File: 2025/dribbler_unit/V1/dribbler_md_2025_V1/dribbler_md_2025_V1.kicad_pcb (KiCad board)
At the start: 2 copper layers, 78 parts, among them J2 Conn_01x07_Pin, J4 Conn_01x02_Pin, J5 Conn_01x02_Pin, J6 Conn_01x04_Pin, U1 MAX3051, U2 DRV8701, U3 STM32F446RETx

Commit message: 回路図完了
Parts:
- added J1: Conn_01x02_Pin, dribbler_md:XT30, F.Cu at (138.5, 53.3)
- added J3: Conn_01x02_Pin, dribbler_md:XT30, F.Cu at (145.2, 53.3)
- added R34: 10k, Resistor_SMD:R_0603_1608Metric_Pad0.98x0.95mm_HandSolder, F.Cu at (128.2, 62.1)
- added SW1: SW_Wuerth_450301014042, dribbler_md:IS-1235-G, F.Cu at (109.9, 108.2)
- added SW2: SW_Wuerth_450301014042, dribbler_md:IS-1235-G, F.Cu at (123.2, 108.2)
- added SW3: SW_MEC_5E, dribbler_md:TS-06104, F.Cu at (146.1, 62.5)
- added SW4: SW_Wuerth_450301014042, dribbler_md:IS-1235-G, F.Cu at (135.4, 72.0)
- added SW5: SW_MEC_5E, dribbler_md:TS-06104, F.Cu at (146.1, 69.9)
- added Y1: Crystal_GND2, dribbler_md:CSTNE16M0V530000R0, F.Cu at (124.9, 90.7)
- moved R14 53.2 mm to (176.0, 78.5)
- moved REG1 48.9 mm to (165.1, 95.2)
- moved U2 47.5 mm to (171.6, 70.6)
- moved C3 43.7 mm to (182.5, 86.5)
- moved C2 42.3 mm to (182.5, 58.5)
- moved FET4 40.9 mm to (184.0, 77.7)
- moved FET1 40.6 mm to (183.6, 67.3)
- moved FET2 40.3 mm to (183.4, 71.0)
- moved J2 40.0 mm to (138.1, 43.5)
- moved FET3 39.8 mm to (183.0, 74.7)
- moved J6 29.7 mm to (143.4, 90.8)
- moved J4 28.4 mm to (154.6, 61.6)
- moved J5 28.4 mm to (154.6, 68.1)
- moved C13 26.7 mm to (132.8, 54.3)
- moved C4 26.7 mm to (132.8, 42.3)
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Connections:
- net SN renamed GND_main
- C1 pad 2: MD_SO -> GND_log
- C10 pad 1: MD_SO -> GND_log
- C15 pad 2: MD_SO -> GND_log
- C16 pad 2: MD_SO -> GND_log
- C17 pad 2: MD_SO -> GND_log
- C18 pad 2: MD_SO -> GND_log
- C19 pad 2: MD_SO -> GND_log
- C20 pad 2: MD_SO -> GND_log
- C21 pad 2: MD_SO -> GND_log
- C22 pad 1: MD_SO -> GND_log
- C23 pad 2: MD_SO -> GND_log
- C24 pad 2: MD_SO -> GND_log
- C6 pad 2: MD_SO -> GND_log
- C7 pad 2: MD_SO -> GND_log
- C8 pad 2: MD_SO -> GND_log
- C9 pad 2: MD_SO -> GND_log
- D4 pad 1: MD_SO -> GND_log
- D5 pad 1: MD_SO -> GND_log
- D6 pad 1: MD_SO -> GND_log
- D7 pad 1: MD_SO -> GND_log
- J2 pad 7: MD_SO -> GND_log
- R1 pad 1: MD_SO -> GND_log
- R18 pad 2: MD_SO -> GND_log
- R19 pad 2: MD_SO -> GND_log
- R2 pad 1: MD_SO -> GND_log
- R32 pad 2: MD_SO -> GND_log
- U1 pad 2: MD_SO -> GND_log
- U1 pad 5: MD_SO -> GND_log
- U1 pad 8: MD_SO -> GND_log
- U2 pad 16: MD_SO -> GND_log
- U2 pad 25: MD_SO -> GND_log
- U2 pad 5: MD_SO -> GND_log
- U3 pad 12: MD_SO -> GND_log
- U3 pad 18: MD_SO -> GND_log
- U3 pad 31: MD_SO -> GND_log
- U3 pad 47: MD_SO -> GND_log
- U3 pad 63: MD_SO -> GND_log

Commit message: FET再選定
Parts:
- removed FET1, FET2, FET3, FET4: MCMN2012A-TP, dribbler_md:MCMN2012A
- added C25: 10u, Capacitor_SMD:C_0805_2012Metric_Pad1.18x1.45mm_HandSolder, F.Cu at (197.1, 94.4)
- added C26: 10u, Capacitor_SMD:C_0805_2012Metric_Pad1.18x1.45mm_HandSolder, F.Cu at (197.1, 97.4)
- added C27: 4.7u, Capacitor_SMD:C_0603_1608Metric_Pad1.08x0.95mm_HandSolder, F.Cu at (186.2, 79.7)
- added C28: 0.1u, Capacitor_SMD:C_0603_1608Metric_Pad1.08x0.95mm_HandSolder, F.Cu at (186.2, 82.2)
- added C29: 0.1u, Capacitor_SMD:C_0603_1608Metric_Pad1.08x0.95mm_HandSolder, F.Cu at (186.2, 84.7)
- added C30: 0.1u, Capacitor_SMD:C_0603_1608Metric_Pad1.08x0.95mm_HandSolder, F.Cu at (186.2, 87.2)
- added C31: 0.1u, Capacitor_SMD:C_0603_1608Metric_Pad1.08x0.95mm_HandSolder, F.Cu at (186.2, 89.7)
- added C32: 0.1u, Capacitor_SMD:C_0603_1608Metric_Pad1.08x0.95mm_HandSolder, F.Cu at (186.2, 92.2)
- added C33: 0.1u, Capacitor_SMD:C_0603_1608Metric_Pad1.08x0.95mm_HandSolder, F.Cu at (186.2, 94.8)
- added C34: 4.7u, Capacitor_SMD:C_0603_1608Metric_Pad1.08x0.95mm_HandSolder, F.Cu at (186.2, 97.3)
- added C35: 0.1u, Capacitor_SMD:C_0603_1608Metric_Pad1.08x0.95mm_HandSolder, F.Cu at (186.2, 99.8)
- added C36: 0.1u, Capacitor_SMD:C_0603_1608Metric_Pad1.08x0.95mm_HandSolder, F.Cu at (186.2, 102.3)
- added U4: DRV8701, Package_DFN_QFN:VQFN-24-1EP_4x4mm_P0.5mm_EP2.5x2.5mm, F.Cu at (220.2, 118.8)
- added U5: STM32F446RETx, Package_QFP:LQFP-64_10x10mm_P0.5mm, F.Cu at (195.6, 85.7)
- C10: value 1u -> 10u; footprint Capacitor_SMD:C_0603_1608Metric_Pad1.08x0.95mm_HandSolder -> Capacitor_SMD:C_0805_2012Metric_Pad1.18x1.45mm_HandSolder
- C11, C16, C18, C19, C20, C6, C7: value 0.1u -> 10u; footprint Capacitor_SMD:C_0603_1608Metric_Pad1.08x0.95mm_HandSolder -> Capacitor_SMD:C_0805_2012Metric_Pad1.18x1.45mm_HandSolder
- C12: value 1000pf -> 10u; footprint Capacitor_SMD:C_0603_1608Metric_Pad1.08x0.95mm_HandSolder -> Capacitor_SMD:C_0805_2012Metric_Pad1.18x1.45mm_HandSolder
- C14: value 10u -> 0.1u; footprint Capacitor_SMD:C_0805_2012Metric_Pad1.18x1.45mm_HandSolder -> Capacitor_SMD:C_0603_1608Metric_Pad1.08x0.95mm_HandSolder
- C15: value 4.7u -> 10u; footprint Capacitor_SMD:C_0603_1608Metric_Pad1.08x0.95mm_HandSolder -> Capacitor_SMD:C_0805_2012Metric_Pad1.18x1.45mm_HandSolder
- C2, C3: value 470u -> 10u; footprint Capacitor_SMD:CP_Elec_10x10 -> Capacitor_SMD:C_0805_2012Metric_Pad1.18x1.45mm_HandSolder
- C21: footprint Capacitor_SMD:C_0603_1608Metric_Pad1.08x0.95mm_HandSolder -> Capacitor_SMD:C_0805_2012Metric_Pad1.18x1.45mm_HandSolder
- C22: value 4.7u -> 1u
- C24: value 0.1u -> 1000pf
- C4, C5: value 1u -> 10u
- C9: value 0.1u -> 10u
- F1, F2, REG1: moved to B.Cu
- R1, R10, R13, R15, R2, R3, R4, R5, R6, R7, R8: footprint Resistor_SMD:R_0603_1608Metric_Pad0.98x0.95mm_HandSolder -> Resistor_SMD:R_0402_1005Metric_Pad0.72x0.64mm_HandSolder
- R11, R9: value 10k -> 200; footprint Resistor_SMD:R_0603_1608Metric_Pad0.98x0.95mm_HandSolder -> Resistor_SMD:R_0402_1005Metric_Pad0.72x0.64mm_HandSolder
- R12: value 200 -> 10k; footprint Resistor_SMD:R_0603_1608Metric_Pad0.98x0.95mm_HandSolder -> Resistor_SMD:R_0402_1005Metric_Pad0.72x0.64mm_HandSolder
- R14: value 0.04 -> 10k; footprint Resistor_SMD:R_2512_6332Metric_Pad1.40x3.35mm_HandSolder -> Resistor_SMD:R_0402_1005Metric_Pad0.72x0.64mm_HandSolder; moved to B.Cu
- R16: value 200 -> 0.04; footprint Resistor_SMD:R_0603_1608Metric_Pad0.98x0.95mm_HandSolder -> Resistor_SMD:R_2512_6332Metric_Pad1.40x3.35mm_HandSolder
- R18: value 0 -> 10k
- R22: value 10k -> 0
- R25: value 1k -> 10k; footprint Resistor_SMD:R_0603_1608Metric_Pad0.98x0.95mm_HandSolder -> Resistor_SMD:R_0402_1005Metric_Pad0.72x0.64mm_HandSolder
- R26: value 2k -> 1k
- R27: value 10k -> 2k
- R28: value 1k -> 10k
- R32: value 10k -> 1k
- U2: value DRV8701 -> STS8DN3LLH5; footprint Package_DFN_QFN:VQFN-24-1EP_4x4mm_P0.5mm_EP2.5x2.5mm -> Package_SO:SO-8_3.9x4.9mm_P1.27mm
- U3: value STM32F446RETx -> STS8DN3LLH5; footprint Package_QFP:LQFP-64_10x10mm_P0.5mm -> Package_SO:SO-8_3.9x4.9mm_P1.27mm
- moved R11 129.9 mm to (216.0, 144.1), turned to 90 degrees
- moved R16 128.2 mm to (204.3, 141.8)
- moved R10 127.1 mm to (212.6, 141.1), turned to -90 degrees
- moved R8 126.4 mm to (216.0, 131.2), turned to 90 degrees
- moved R9 125.9 mm to (212.6, 136.9), turned to -90 degrees
- moved C1 121.7 mm to (165.4, 150.8), turned to -90 degrees
- moved R15 121.0 mm to (212.0, 142.7), turned to 180 degrees
- moved R13 119.9 mm to (212.0, 138.5), turned to 180 degrees
- moved R12 119.7 mm to (216.6, 129.7)
- moved R5 114.7 mm to (156.4, 150.6), turned to 90 degrees
- moved R28 114.2 mm to (162.5, 155.9), turned to 180 degrees
- moved R29 113.3 mm to (162.5, 157.6), turned to 180 degrees
- moved R30 101.6 mm to (177.7, 140.8)
- moved R31 101.6 mm to (177.7, 143.3)
- moved J2 101.5 mm to (152.5, 144.0), turned to 90 degrees
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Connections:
- C10 pad 1: GND_log -> 18V_main
- C10 pad 2: Net-(U2-VCP) -> GND_main
- C11 pad 1: Net-(U2-CPH) -> 18V_main
- C11 pad 2: Net-(U2-CPL) -> GND_main
- C12 pad 1: SP -> 18V_main
- C13 pad 1: Net-(REG1-VIN) -> 18V_main
- C13 pad 2: GND_REG -> GND_main
- C14 pad 1: 3.3V_sub -> Net-(U4-AVDD)
- C14 pad 2: GND_REG -> GND_log
- C15 pad 1: Net-(U3-VCAP_1) -> 18V_main
- C15 pad 2: GND_log -> GND_main
- C16 pad 1: 3.3V_sub -> 18V_main
- C16 pad 2: GND_log -> GND_main
- C17 pad 1: 3.3V_sub -> Net-(U4-DVDD)
- C18 pad 1: 3.3V_sub -> 18V_main
- C18 pad 2: GND_log -> GND_main
- C19 pad 1: 3.3V_sub -> 18V_main
- C19 pad 2: GND_log -> GND_main
- C20 pad 1: 3.3V_sub -> 18V_main
- C21 pad 1: 3.3V_sub -> 18V_main
- C22 pad 2: 3.3V_sub -> Net-(U4-VCP)
- C23 pad 1: NRST -> Net-(U4-CPH)
- C23 pad 2: GND_log -> Net-(U4-CPL)
- C24 pad 1: USER_SW -> SP
- C24 pad 2: GND_log -> GND_main
- C6 pad 1: Net-(U2-AVDD) -> 18V_main
- C6 pad 2: GND_log -> GND_main
- C7 pad 1: Net-(U2-DVDD) -> 18V_main
- C7 pad 2: GND_log -> GND_main
- C8 pad 2: GND_log -> GND_main
- C9 pad 2: GND_log -> GND_main
- R10 pad 1: SP -> Net-(U2-G2)
- R10 pad 2: Net-(FET3-gate) -> SP
- R11 pad 1: SH1 -> Net-(U2-G2)
- R11 pad 2: Net-(FET4-gate) -> GL2
- R12 pad 1: Net-(FET1-gate) -> Net-(U3-G1)
- R12 pad 2: GH2 -> SP
- R13 pad 1: Net-(FET2-gate) -> Net-(U3-G1)
- R13 pad 2: GL2 -> GL1
- R14 pad 1: SP -> Net-(U3-G2)
- R14 pad 2: GND_main -> SH1
- R15 pad 1: Net-(FET3-gate) -> Net-(U3-G2)
- R15 pad 2: GL1 -> GH1
- R16 pad 1: Net-(FET4-gate) -> SP
- R16 pad 2: GH1 -> GND_main
- R17 pad 1: Net-(U2-SO) -> Net-(U4-SO)
- R18 pad 1: GND_main -> MD_SO
- R20 pad 2: GND_REG -> GND_log
- R22 pad 2: ENC_1 -> GND_REG
- R23 pad 1: ENC_2 -> GND_main
- R23 pad 2: GND_main -> ENC_1
- R24 pad 1: 3.3V_sub -> ENC_2
- R24 pad 2: NRST -> GND_main
- R25 pad 2: Net-(D1-A) -> NRST
- R26 pad 1: 6.5V_main -> 3.3V_sub
- R26 pad 2: Net-(D2-A) -> Net-(D1-A)
- R27 pad 1: 18V_main -> 6.5V_main
- R27 pad 2: Net-(D3-A) -> Net-(D2-A)
- R28 pad 1: USER_LED_1 -> 18V_main
- R28 pad 2: Net-(D4-A) -> Net-(D3-A)
- R29 pad 1: USER_LED_2 -> USER_LED_1
- R29 pad 2: Net-(D5-A) -> Net-(D4-A)
- R3 pad 2: Net-(U2-AVDD) -> Net-(U4-AVDD)
- R30 pad 1: GL2 -> USER_LED_2
- R30 pad 2: Net-(D6-A) -> Net-(D5-A)
- R31 pad 1: GL1 -> GL2
- R31 pad 2: Net-(D7-A) -> Net-(D6-A)
- R32 pad 1: BOOT -> GL1
- R32 pad 2: GND_log -> Net-(D7-A)
- R33 pad 1: 3.3V_sub -> BOOT
- R33 pad 2: USER_SW -> GND_log
- R34 pad 1: MD_SO -> 3.3V_sub
- R34 pad 2: GND_log -> USER_SW
- R4 pad 2: Net-(U2-AVDD) -> Net-(U4-AVDD)
- R6 pad 1: Net-(U2-nFAULT) -> Net-(U4-nFAULT)
- R7 pad 2: Net-(U2-SNSOUT) -> Net-(U4-SNSOUT)
- R8 pad 1: SH2 -> Net-(U2-G1)
- R8 pad 2: Net-(FET1-gate) -> SH2
- R9 pad 1: SP -> Net-(U2-G1)
- R9 pad 2: Net-(FET2-gate) -> GH2
- U2 pad 1: 18V_main -> SH2
- U2 pad 2: Net-(U2-VCP) -> Net-(U2-G1)
- U2 pad 3: Net-(U2-CPH) -> SP
- U2 pad 4: Net-(U2-CPL) -> Net-(U2-G2)
- U2 pad 5: GND_log -> SH2
- U2 pad 6: MD_VREF -> SH2
- U2 pad 7: Net-(U2-AVDD) -> 18V_main
- U2 pad 8: Net-(U2-DVDD) -> 18V_main
- U3 pad 1: 3.3V_sub -> SP
- U3 pad 2: unconnected-(U3-PC13-Pad2) -> Net-(U3-G1)
- U3 pad 3: unconnected-(U3-PC14-Pad3) -> SH1
- U3 pad 4: unconnected-(U3-PC15-Pad4) -> Net-(U3-G2)
- U3 pad 5: Net-(U3-PH0) -> 18V_main
- U3 pad 6: Net-(U3-PH1) -> 18V_main
- U3 pad 7: NRST -> SH1
- U3 pad 8: unconnected-(U3-PC0-Pad8) -> SH1
- Y1 pad 1: Net-(U3-PH0) -> Net-(U5-PH0)
- Y1 pad 3: Net-(U3-PH1) -> Net-(U5-PH1)
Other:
- board outline added: 50 x 50 mm

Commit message: FET周りを配線
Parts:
- added REF**: m2 hole, dribbler_md:m2 hole, F.Cu at (187.0, 103.0)
- added REF**: m2 hole, dribbler_md:m2 hole, F.Cu at (143.0, 147.0)
- added REF**: m2 hole, dribbler_md:m2 hole, F.Cu at (187.0, 147.0)
- added REF**: m2 hole, dribbler_md:m2 hole, F.Cu at (143.0, 103.0)
- F1, F2, R14, REG1: moved to F.Cu
- moved C1 121.4 mm to (88.6, 56.8), turned to 0 degrees
- moved R29 117.7 mm to (101.7, 56.8), turned to 0 degrees
- moved R31 111.5 mm to (101.7, 61.8)
- moved R30 111.5 mm to (101.7, 59.3)
- moved R28 102.5 mm to (97.3, 76.9), turned to 0 degrees
- moved C30 98.0 mm to (93.0, 56.8)
- moved C31 98.0 mm to (93.0, 59.3)
- moved C32 98.0 mm to (93.0, 61.8)
- moved C33 98.0 mm to (93.0, 64.3)
- moved C34 98.0 mm to (93.0, 66.8)
- moved C35 98.0 mm to (93.0, 69.3)
- moved C36 98.0 mm to (93.0, 71.8)
- moved C27 97.9 mm to (88.6, 71.8)
- moved C28 97.9 mm to (88.6, 74.3)
- moved C29 97.9 mm to (88.6, 76.9)
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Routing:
- net Net-(U2-G2): track 0.00 -> 4.11 mm
- net Net-(U3-G1): track 0.00 -> 4.11 mm
- net Net-(U3-G2): track 0.00 -> 4.11 mm
- net Net-(U2-G1): track 0.00 -> 4.11 mm
- added copper zone on F.Cu, net 18V_main
- added copper zone on F.Cu, net SH1
- added copper zone on F.Cu, net SH2
- added copper zone on F.Cu, net SP

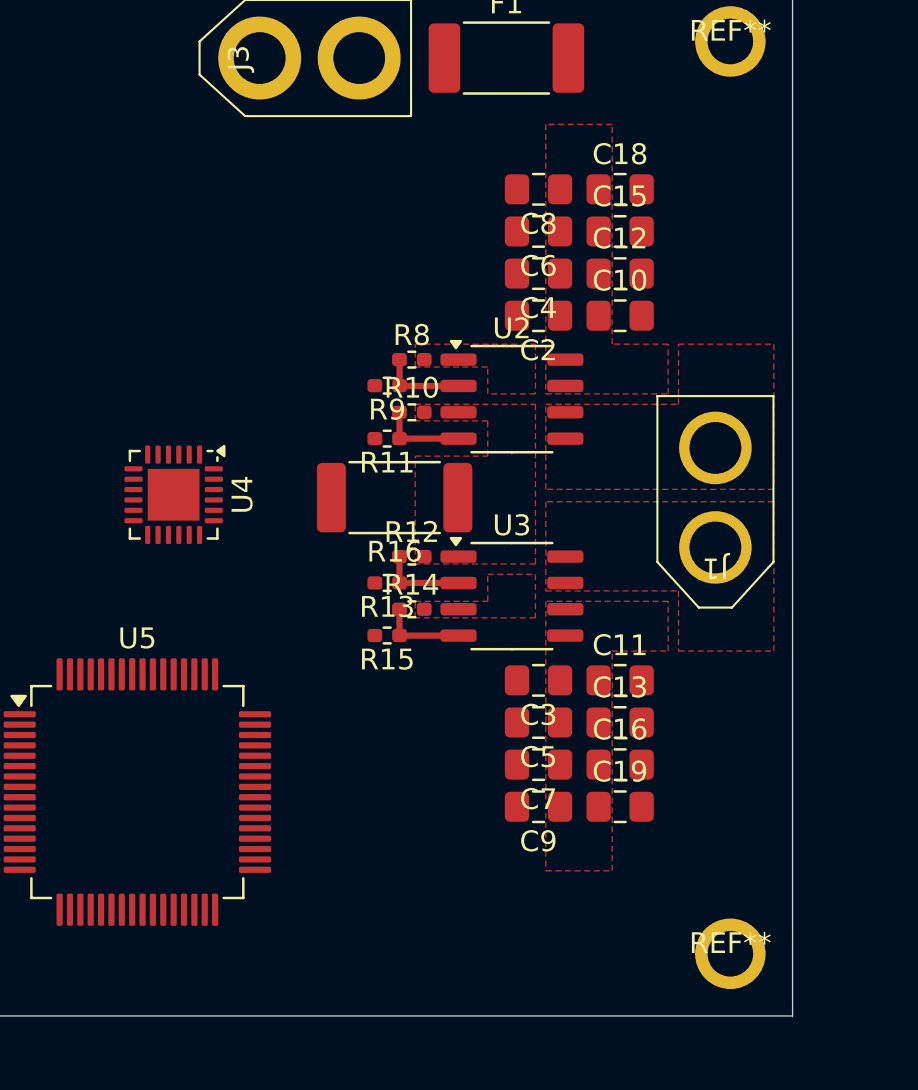
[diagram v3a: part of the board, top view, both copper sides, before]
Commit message: FET周りを配線-2
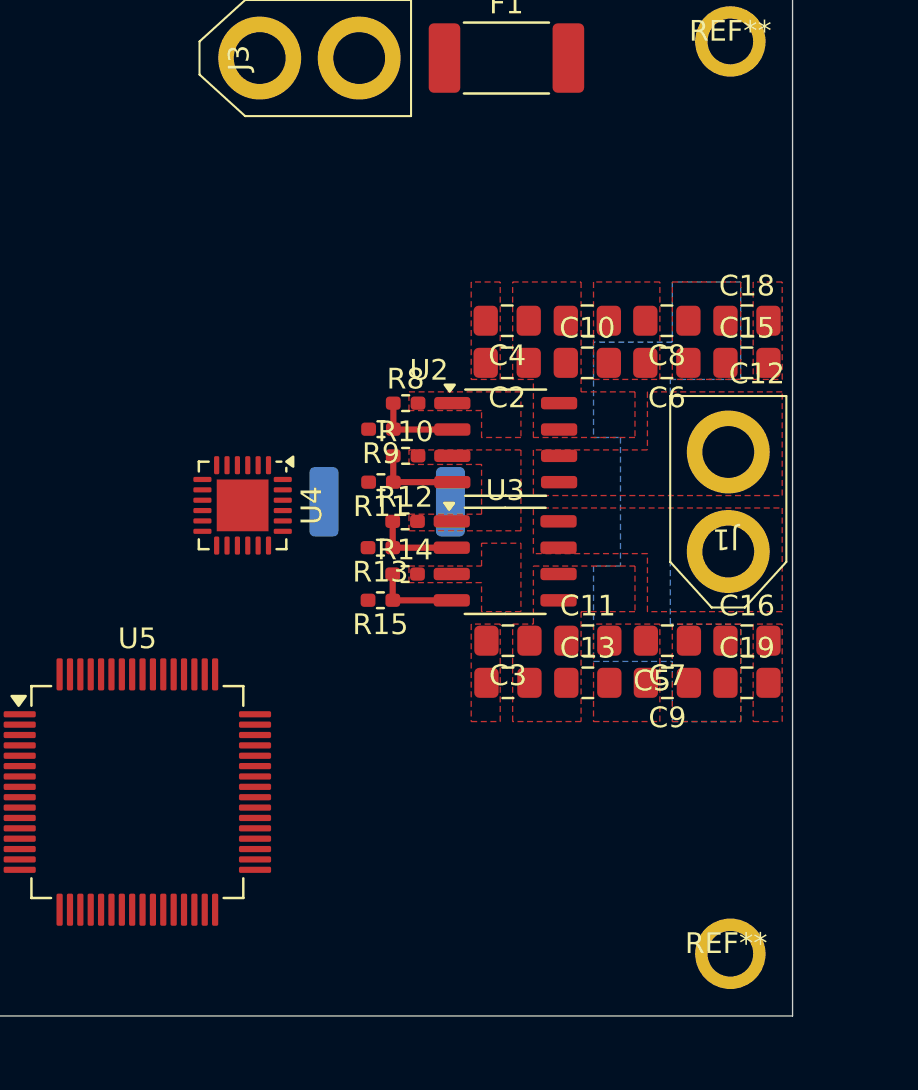
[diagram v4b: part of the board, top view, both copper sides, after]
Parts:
- R16: moved to B.Cu
- moved C6 8.86 mm to (183.9, 118.5)
- moved C8 8.86 mm to (183.9, 116.5)
- moved C15 8.81 mm to (187.8, 118.5)
- moved C18 8.81 mm to (187.8, 116.5)
- moved C7 8.62 mm to (184.0, 131.9)
- moved C9 8.62 mm to (184.0, 133.9)
- moved C16 8.55 mm to (187.8, 131.9)
- moved C19 8.55 mm to (187.8, 133.9)
- moved U4 3.36 mm to (163.5, 125.4)
- moved C10 2.77 mm to (180.1, 118.5)
- moved C12 2.77 mm to (180.1, 116.5)
- moved C2 2.73 mm to (176.2, 118.5)
- moved C4 2.73 mm to (176.2, 116.5)
- moved C13 2.47 mm to (180.1, 133.9)
- moved C11 2.47 mm to (180.1, 131.9)
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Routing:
- added copper zone on B.Cu, net 18V_main
- added copper zone on F.Cu, net GND_main

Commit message: FETの配線終わり
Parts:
- C24: footprint Capacitor_SMD:C_0603_1608Metric_Pad1.08x0.95mm_HandSolder -> Capacitor_SMD:C_0805_2012Metric_Pad1.18x1.45mm_HandSolder
- moved C24 95.2 mm to (165.9, 125.0)
- moved C22 91.1 mm to (160.7, 119.9), turned to -90 degrees
- moved C17 90.9 mm to (155.2, 123.7), turned to 180 degrees
- moved C23 87.9 mm to (158.7, 119.9), turned to -90 degrees
- moved C20 73.0 mm to (162.5, 119.9), turned to 90 degrees
- moved C21 71.8 mm to (164.5, 119.9), turned to 90 degrees
- moved R1 60.5 mm to (157.9, 129.1), turned to 90 degrees
- moved R3 56.7 mm to (156.9, 129.1), turned to -90 degrees
- moved R7 54.4 mm to (154.6, 126.0)
- moved R17 51.4 mm to (155.2, 127.3), turned to 180 degrees
- moved R2 50.8 mm to (156.7, 119.8), turned to -90 degrees
- moved R6 47.3 mm to (154.6, 125.0), turned to 180 degrees
- moved R4 47.1 mm to (155.7, 119.8), turned to 90 degrees
- moved C14 38.2 mm to (155.2, 122.2), turned to 180 degrees
- moved F2 36.1 mm to (162.1, 83.4), turned to 90 degrees
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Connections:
- REG1 pad 4: GND_REG -> (no net)
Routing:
- net 18V_main: track 0.00 -> 21.7 mm, vias 0 -> 20
- net Net-(U4-AVDD): track 0.00 -> 17.5 mm, vias 0 -> 2
- net SH1: track 0.00 -> 17.3 mm, vias 0 -> 14
- net SH2: track 0.00 -> 12.7 mm, vias 0 -> 12
- net SP: track 0.00 -> 11.6 mm, vias 0 -> 10
- net GND_main: track 0.00 -> 11.6 mm, vias 0 -> 18
- net GH1: track 0.00 -> 10.8 mm
- net GH2: track 0.00 -> 9.26 mm, vias 0 -> 2
- net GL1: track 0.00 -> 9.10 mm
- net GL2: track 0.00 -> 8.52 mm
- net Net-(U4-CPH): track 0.00 -> 4.42 mm
- net MD_VREF: track 0.00 -> 4.29 mm
- net MD_IDRIVE: track 0.00 -> 3.48 mm
- net Net-(U4-SNSOUT): track 0.00 -> 2.61 mm
- net Net-(U4-CPL): track 0.00 -> 2.50 mm
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- added copper zone on B.Cu, net GND_main
- added copper zone on B.Cu, net SH1
- added copper zone on B.Cu, net SH2
- added copper zone on B.Cu, net SP

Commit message: 4461周りを配線途中
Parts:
- C24, C25, C26, C35, C36, F1, F2, R23, R24, R34, REG1: moved to B.Cu
- R25: footprint Resistor_SMD:R_0402_1005Metric_Pad0.72x0.64mm_HandSolder -> Resistor_SMD:R_0603_1608Metric_Pad0.98x0.95mm_HandSolder; moved to B.Cu
- moved R29 116.8 mm to (118.5, 172.4)
- moved C31 98.1 mm to (166.2, 124.6), turned to -90 degrees
- moved C28 96.0 mm to (164.8, 132.8)
- moved C30 94.0 mm to (150.4, 131.2), turned to 180 degrees
- moved C29 93.6 mm to (164.8, 131.2)
- moved C32 88.4 mm to (161.2, 118.0)
- moved R19 87.6 mm to (167.7, 109.0), turned to 180 degrees
- moved R20 87.1 mm to (167.7, 110.6), turned to 180 degrees
- moved C1 81.7 mm to (152.4, 107.8)
- moved C35 81.5 mm to (166.7, 104.0)
- moved R23 81.2 mm to (146.3, 131.6), turned to 180 degrees
- moved C33 80.7 mm to (151.6, 119.8), turned to 180 degrees
- moved C27 79.3 mm to (153.4, 117.6), turned to 180 degrees
- moved R24 77.7 mm to (146.3, 129.6)
- moved SW1 75.4 mm to (179.2, 137.2), turned to 180 degrees
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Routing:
- net USER_SW: track 0.00 -> 48.3 mm, vias 0 -> 2
- net NRST: track 0.00 -> 33.6 mm, vias 0 -> 2
- net Net-(REG1-VIN): track 0.00 -> 25.7 mm
- net CANH: track 0.00 -> 23.0 mm
- net CANL: track 0.00 -> 23.0 mm
- net 3.3V_sub: track 1.02 -> 21.9 mm
- net 18V_main: track 21.7 -> 4.88 mm
- net Net-(SW1-B): track 0.00 -> 13.2 mm
- net 6.5V_main: track 0.00 -> 12.8 mm
- net Net-(U4-AVDD): track 17.5 -> 28.3 mm
- net SP: track 11.6 -> 4.39 mm, vias 10 -> 11
- net Net-(U5-PH0): track 0.00 -> 5.04 mm
- net MD_IN2: track 0.00 -> 4.92 mm
- net MD_IN1: track 0.00 -> 4.92 mm
- net SH1: track 17.3 -> 21.6 mm
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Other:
- board size 50 x 50 mm -> 50 x 40 mm
